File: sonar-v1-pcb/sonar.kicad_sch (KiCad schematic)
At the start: 1 part

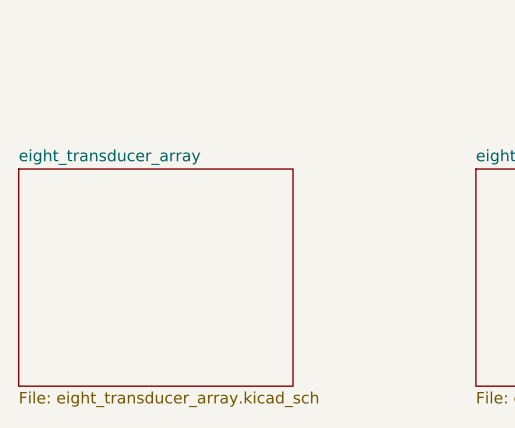
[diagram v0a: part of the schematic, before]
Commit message: Update gitignore and save schematic/PCB progress
Co-Authored-By: Claude Opus 4.6 <noreply@anthropic.com>
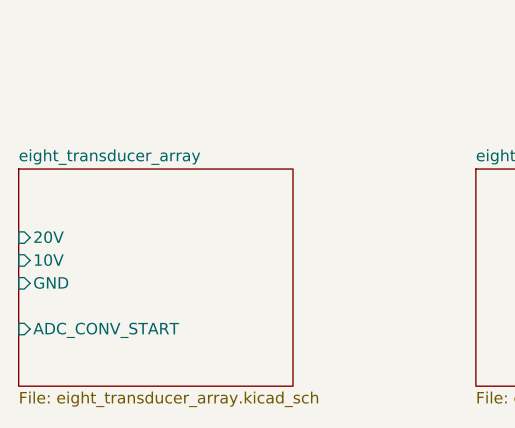
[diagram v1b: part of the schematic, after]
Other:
- sheet eight_transducer_array ports: added 10V, 20V, ADC_CONV_START, GND; removed none
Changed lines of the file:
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@@
+			)
+		)
+		(pin "GND" input
+			(at 64.77 127 180)
+			(effects
+				(font
+					(size 1.27 1.27)
+				)
+				(justify left)
+			)
+		)
+		(pin "20V" input
+			(at 64.77 121.92 180)
+			(effects
+				(font
+					(size 1.27 1.27)
+				)
+				(justify left)
+			)
+		)
+		(pin "ADC_CONV_START" input
+			(at 64.77 132.08 180)
+			(effects
+				(font
+					(size 1.27 1.27)
+				)
+				(justify left)
+			)
+		)
+		(pin "10V" input
+			(at 64.77 124.46 180)
+			(effects
+				(font
+					(size 1.27 1.27)
+				)
+				(justify left)
 			)
 		)
